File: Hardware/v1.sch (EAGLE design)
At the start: 75 parts, among them IC1 LM324D, IC2 m328p, IC3 REG1117, J1 22-27-2061-06, J2 22-27-2021-02, J3 22-27-2021-02, J4 22-27-2031-03, J5 22-27-2041-04, Q1 BSS123, Q2 BSS123, Q3 BSS123, Q5 BSS123

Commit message: slight changes in the layout
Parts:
- C9: value (none) -> 1000u
- L1, L2: device rcl:L-EUL2012C -> rcl:L-EUL2825P
- U$1: device IRF7424:IRF7424 -> MyLib:IRF7424
- U$3: value ELKO-1,27-4,2 -> 330u; device MyLib:ELKO-1,27-4,2 -> rcl:CPOL-EUE2-5
- U$4: value ELKO-1,27-4,2 -> 330u; device MyLib:ELKO-1,27-4,2 -> rcl:CPOL-EUE3.5-8
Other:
- moved on the sheet: C9, U$1
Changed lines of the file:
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@@
 <?xml version="1.0" encoding="utf-8"?>
 <!DOCTYPE eagle SYSTEM "eagle.dtd">
-<eagle version="6.6.0">
+<eagle version="6.5.0">
 <drawing>
 <settings>
@@
 <part name="S4" library="switch-omron" deviceset="10-XX" device=""/>
 <part name="GND4" library="supply1" deviceset="GND" device=""/>
-<part name="U$1" library="IRF7424" deviceset="IRF7424" device=""/>
+<part name="U$1" library="MyLib" deviceset="IRF7424" device=""/>
 <part name="U$2" library="3x7segCC" deviceset="3X7SEG" device=""/>
 <part name="GND5" library="supply1" deviceset="GND" device=""/>
@@
 <part name="R6" library="rcl" deviceset="R-EU_" device="R0402" value="10k"/>
 <part name="R7" library="rcl" deviceset="R-EU_" device="R0402" value="10k"/>
-<part name="U$3" library="MyLib" deviceset="ELKO-1,27-4,2" device=""/>
+<part name="U$3" library="rcl" deviceset="CPOL-EU" device="E2-5" value="330u"/>
 <part name="TP1" library="testpad" deviceset="PTR1" device="B1,27"/>
 <part name="TP2" library="testpad" deviceset="PTR1" device="B1,27"/>
@@
 <part name="TP5" library="testpad" deviceset="PTR1" device="B1,27"/>
 <part name="GND3" library="supply1" deviceset="GND" device=""/>
-<part name="L1" library="rcl" deviceset="L-EU" device="L2012C" value="10u"/>
-<part name="L2" library="rcl" deviceset="L-EU" device="L2012C" value="10u"/>
+<part name="L1" library="rcl" deviceset="L-EU" device="L2825P" value="10u"/>
+<part name="L2" library="rcl" deviceset="L-EU" device="L2825P" value="10u"/>
 <part name="C2" library="rcl" deviceset="C-EU" device="C0603" value="100n"/>
 <part name="GND12" library="supply1" deviceset="GND" device=""/>
@@
 <part name="TP9" library="testpad" deviceset="PTR1" device="B1,27"/>
 <part name="TP10" library="testpad" deviceset="PTR1" device="B1,27"/>
-<part name="C9" library="rcl" deviceset="CPOL-EU" device="E5-13"/>
+<part name="C9" library="rcl" deviceset="CPOL-EU" device="E5-13" value="1000u"/>
 <part name="R24" library="rcl" deviceset="R-EU_" device="R0603" value="750k"/>
 <part name="R25" library="rcl" deviceset="R-EU_" device="R0603" value="1k2"/>
@@
 <part name="J5" library="con-molex" deviceset="22-?-04" device="27-2041"/>
 <part name="J2" library="con-molex" deviceset="22-?-02" device="27-2021"/>
-<part name="U$4" library="MyLib" deviceset="ELKO-1,27-4,2" device=""/>
+<part name="U$4" library="rcl" deviceset="CPOL-EU" device="E3.5-8" value="330u"/>
 </parts>
 <sheets>
@@
 <instance part="S4" gate="1" x="304.8" y="238.76" rot="R270"/>
 <instance part="GND4" gate="1" x="210.82" y="200.66"/>
-<instance part="U$1" gate="G$1" x="190.5" y="223.52"/>
+<instance part="U$1" gate="G$1" x="167.64" y="208.28"/>
 <instance part="U$2" gate="G$1" x="223.52" y="48.26"/>
 <instance part="GND5" gate="1" x="76.2" y="218.44"/>
@@
 <instance part="TP9" gate="G$1" x="124.46" y="114.3" rot="R270"/>
 <instance part="TP10" gate="G$1" x="124.46" y="116.84" rot="R270"/>
-<instance part="C9" gate="G$1" x="180.34" y="210.82"/>
+<instance part="C9" gate="G$1" x="177.8" y="210.82"/>
 <instance part="IC1" gate="B" x="58.42" y="5.08"/>
 <instance part="R24" gate="G$1" x="55.88" y="-7.62"/>
@@
 <pinref part="J1" gate="-3" pin="S"/>
 <pinref part="C9" gate="G$1" pin="-"/>
-<wire x1="180.34" y1="205.74" x2="210.82" y2="205.74" width="0.1524" layer="91"/>
+<wire x1="177.8" y1="205.74" x2="210.82" y2="205.74" width="0.1524" layer="91"/>
 <junction x="210.82" y="205.74"/>
 <pinref part="C12" gate="G$1" pin="2"/>
-<wire x1="180.34" y1="205.74" x2="172.72" y2="205.74" width="0.1524" layer="91"/>
-<junction x="180.34" y="205.74"/>
+<wire x1="177.8" y1="205.74" x2="172.72" y2="205.74" width="0.1524" layer="91"/>
+<junction x="177.8" y="205.74"/>
 </segment>
 <segment>
@@
 <wire x1="177.8" y1="226.06" x2="177.8" y2="220.98" width="0.1524" layer="91"/>
 <junction x="177.8" y="220.98"/>
-<wire x1="177.8" y1="220.98" x2="180.34" y2="213.36" width="0.1524" layer="91"/>
+<wire x1="177.8" y1="220.98" x2="177.8" y2="218.44" width="0.1524" layer="91"/>
 <pinref part="C12" gate="G$1" pin="1"/>
-<wire x1="172.72" y1="213.36" x2="180.34" y2="213.36" width="0.1524" layer="91"/>
-<junction x="180.34" y="213.36"/>
+<wire x1="172.72" y1="213.36" x2="177.8" y2="213.36" width="0.1524" layer="91"/>
+<junction x="177.8" y="213.36"/>
+<wire x1="177.8" y1="218.44" x2="180.34" y2="218.44" width="0.1524" layer="91"/>
+<wire x1="180.34" y1="218.44" x2="180.34" y2="213.36" width="0.1524" layer="91"/>
+<wire x1="180.34" y1="213.36" x2="177.8" y2="213.36" width="0.1524" layer="91"/>
 </segment>
 </net>
@@
 <wire x1="208.28" y1="213.36" x2="218.44" y2="213.36" width="0.1524" layer="91"/>
 <pinref part="U$1" gate="G$1" pin="D1"/>
+<wire x1="200.66" y1="231.14" x2="203.2" y2="231.14" width="0.1524" layer="91"/>
 <pinref part="U$1" gate="G$1" pin="D2"/>
+<wire x1="200.66" y1="226.06" x2="203.2" y2="226.06" width="0.1524" layer="91"/>
 <junction x="203.2" y="226.06"/>
 <pinref part="U$1" gate="G$1" pin="D3"/>
+<wire x1="200.66" y1="220.98" x2="203.2" y2="220.98" width="0.1524" layer="91"/>
 <junction x="203.2" y="220.98"/>
 <pinref part="U$1" gate="G$1" pin="D4"/>
+<wire x1="200.66" y1="215.9" x2="203.2" y2="215.9" width="0.1524" layer="91"/>
 <wire x1="218.44" y1="215.9" x2="218.44" y2="213.36" width="0.1524" layer="91"/>
 <pinref part="LED1" gate="G$1" pin="A"/>

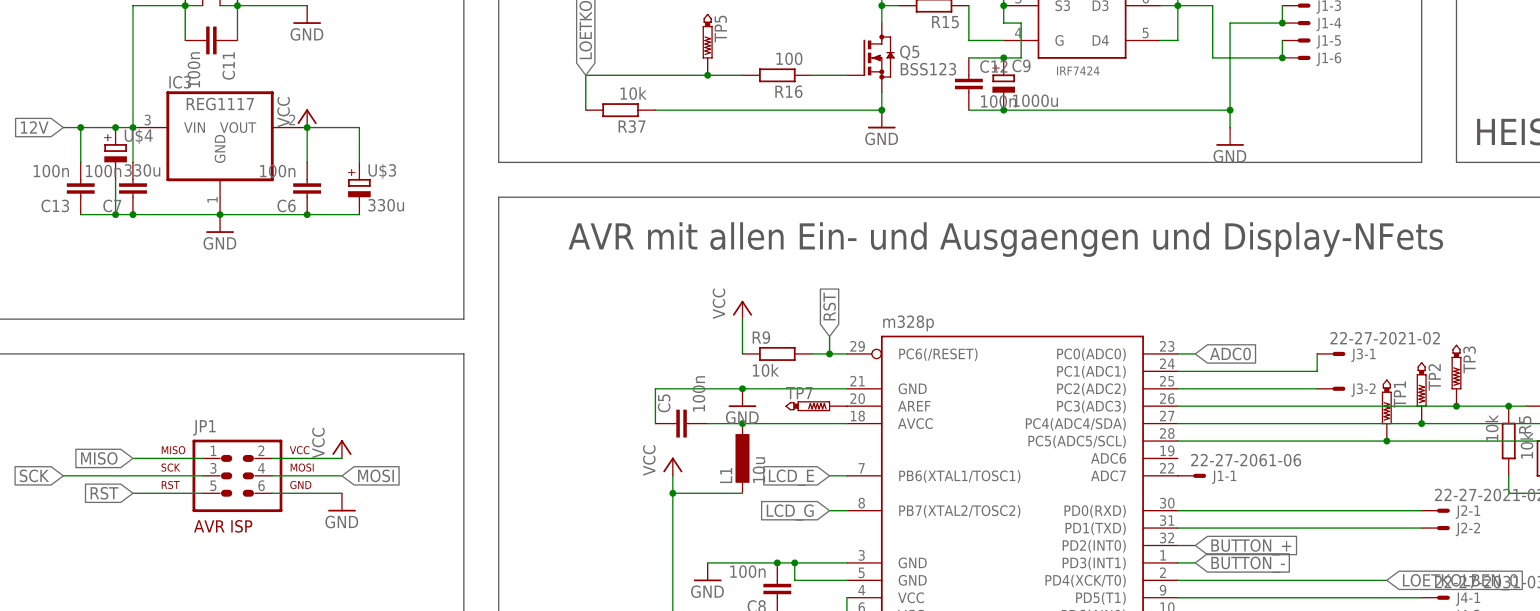
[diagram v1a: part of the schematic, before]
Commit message: finish layer done so pcb will have the components names printed on it
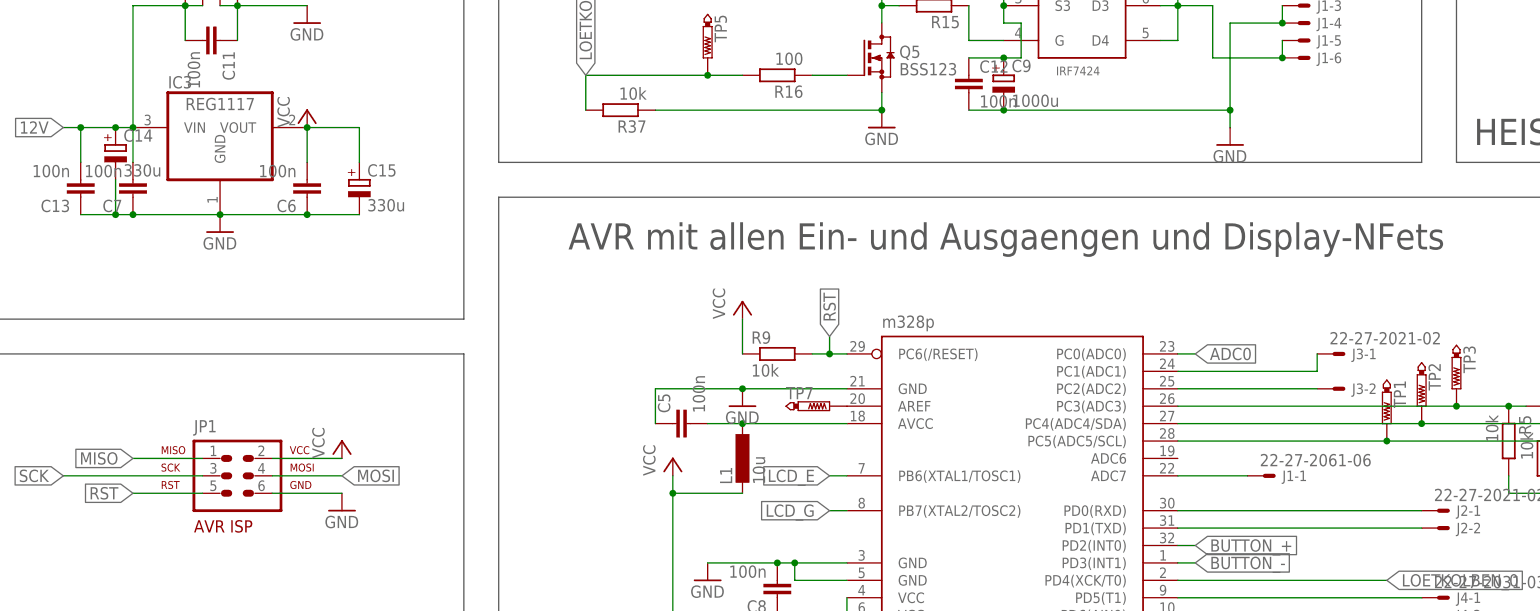
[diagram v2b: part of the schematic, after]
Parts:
- renumbered U$3 to C15, U$4 to C14
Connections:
- net N$27 renamed ADC7
- net N$28 renamed ADC1
- net N$29 renamed ADC2
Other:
- moved on the sheet: J1-1
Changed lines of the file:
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@@
 <part name="R6" library="rcl" deviceset="R-EU_" device="R0402" value="10k"/>
 <part name="R7" library="rcl" deviceset="R-EU_" device="R0402" value="10k"/>
-<part name="U$3" library="rcl" deviceset="CPOL-EU" device="E2-5" value="330u"/>
+<part name="C15" library="rcl" deviceset="CPOL-EU" device="E2-5" value="330u"/>
 <part name="TP1" library="testpad" deviceset="PTR1" device="B1,27"/>
 <part name="TP2" library="testpad" deviceset="PTR1" device="B1,27"/>
@@
 <part name="J5" library="con-molex" deviceset="22-?-04" device="27-2041"/>
 <part name="J2" library="con-molex" deviceset="22-?-02" device="27-2021"/>
-<part name="U$4" library="rcl" deviceset="CPOL-EU" device="E3.5-8" value="330u"/>
+<part name="C14" library="rcl" deviceset="CPOL-EU" device="E3.5-8" value="330u"/>
 </parts>
 <sheets>
@@
 <instance part="R6" gate="G$1" x="256.54" y="154.94" rot="R270"/>
 <instance part="R7" gate="G$1" x="261.62" y="152.4" rot="R270"/>
-<instance part="U$3" gate="G$1" x="83.82" y="195.58"/>
+<instance part="C15" gate="G$1" x="83.82" y="195.58"/>
 <instance part="TP1" gate="G$1" x="233.68" y="160.02" rot="R180"/>
 <instance part="TP2" gate="G$1" x="238.76" y="162.56" rot="R180"/>
@@
 <instance part="R26" gate="G$1" x="208.28" y="238.76" rot="R180"/>
 <instance part="GND18" gate="1" x="213.36" y="236.22"/>
-<instance part="J1" gate="-1" x="205.74" y="152.4"/>
+<instance part="J1" gate="-1" x="215.9" y="152.4"/>
 <instance part="J1" gate="-2" x="220.98" y="223.52"/>
 <instance part="J1" gate="-3" x="220.98" y="220.98"/>
@@
 <instance part="J2" gate="-1" x="241.3" y="147.32"/>
 <instance part="J2" gate="-2" x="241.3" y="144.78"/>
-<instance part="U$4" gate="G$1" x="48.26" y="200.66"/>
+<instance part="C14" gate="G$1" x="48.26" y="200.66"/>
 </instances>
 <busses>
@@
 <pinref part="P+5" gate="VCC" pin="VCC"/>
 <junction x="76.2" y="203.2"/>
-<pinref part="U$3" gate="G$1" pin="+"/>
+<pinref part="C15" gate="G$1" pin="+"/>
 <wire x1="76.2" y1="203.2" x2="83.82" y2="203.2" width="0.1524" layer="91"/>
 <wire x1="83.82" y1="203.2" x2="83.82" y2="198.12" width="0.1524" layer="91"/>
@@
 <junction x="63.5" y="190.5"/>
 <pinref part="GND15" gate="1" pin="GND"/>
-<pinref part="U$3" gate="G$1" pin="-"/>
+<pinref part="C15" gate="G$1" pin="-"/>
 <wire x1="83.82" y1="190.5" x2="76.2" y2="190.5" width="0.1524" layer="91"/>
 <junction x="76.2" y="190.5"/>
@@
 <wire x1="43.18" y1="190.5" x2="48.26" y2="190.5" width="0.1524" layer="91"/>
 <junction x="50.8" y="190.5"/>
-<pinref part="U$4" gate="G$1" pin="-"/>
+<pinref part="C14" gate="G$1" pin="-"/>
 <wire x1="48.26" y1="190.5" x2="50.8" y2="190.5" width="0.1524" layer="91"/>
 <wire x1="48.26" y1="195.58" x2="48.26" y2="190.5" width="0.1524" layer="91"/>
@@
 <pinref part="J5" gate="-1" pin="S"/>
 <pinref part="J5" gate="-2" pin="S"/>
-<pinref part="U$4" gate="G$1" pin="+"/>
+<pinref part="C14" gate="G$1" pin="+"/>
 <junction x="48.26" y="203.2"/>
 </segment>
@@
 </segment>
 </net>
-<net name="N$27" class="0">
+<net name="ADC7" class="0">
 <segment>
 <pinref part="IC2" gate="G$1" pin="ADC7"/>
 <pinref part="J1" gate="-1" pin="S"/>
-</segment>
-</net>
-<net name="N$28" class="0">
+<wire x1="213.36" y1="152.4" x2="203.2" y2="152.4" width="0.1524" layer="91"/>
+</segment>
+</net>
+<net name="ADC1" class="0">
 <segment>
 <pinref part="IC2" gate="G$1" pin="PC1(ADC1)"/>
@@
 </segment>
 </net>
-<net name="N$29" class="0">
+<net name="ADC2" class="0">
 <segment>
 <pinref part="J3" gate="-2" pin="S"/>

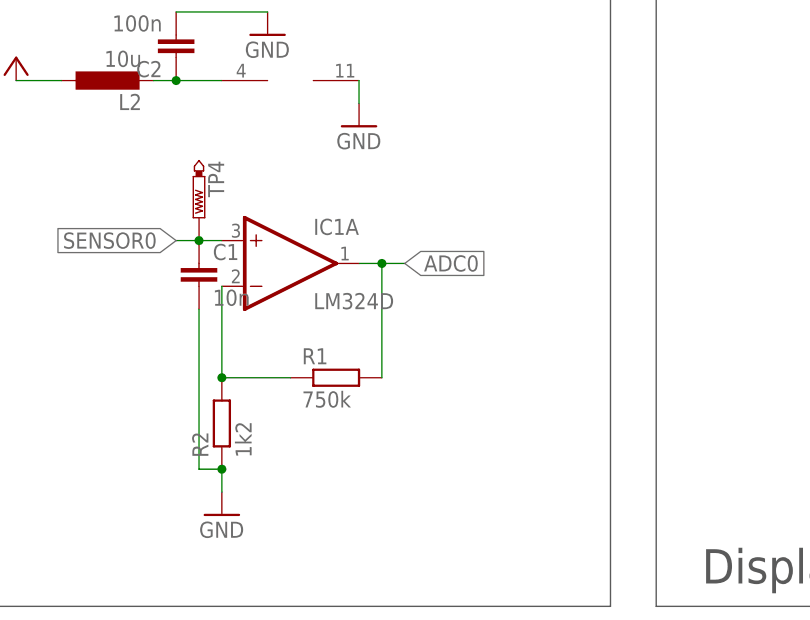
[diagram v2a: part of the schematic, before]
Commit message: op-amp rework
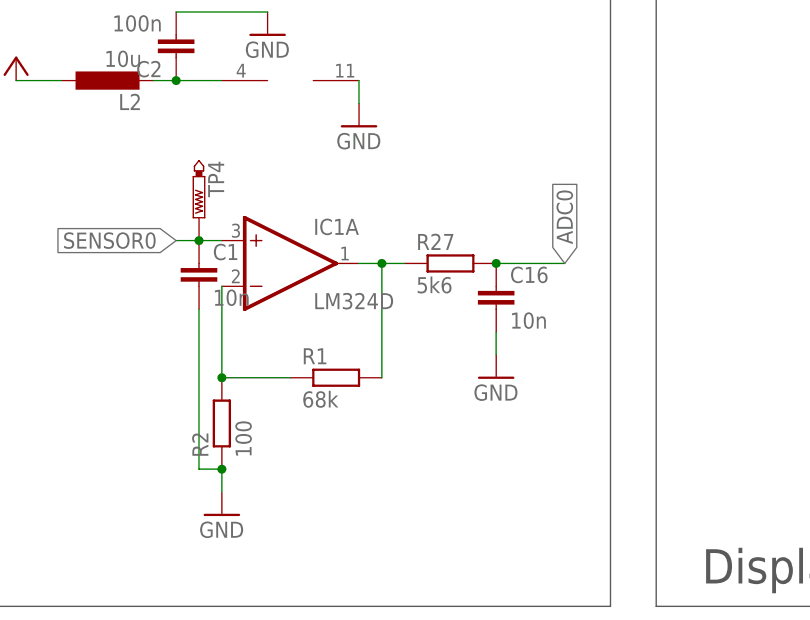
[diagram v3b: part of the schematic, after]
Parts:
- added C16: 10n, rcl:C-EUC0603
- added R27: 5k6, rcl:R-EU_R0603
- R1: value 750k -> 68k
- R2: value 1k2 -> 100
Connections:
- new net SDFGHJK: IC1A.OUT, R1.2, R27.1
- net ADC0: now also C16.1, R27.2; no longer IC1A.OUT, R1.2
- net GND: now also C16.2
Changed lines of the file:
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@@
 <part name="P+1" library="supply1" deviceset="VCC" device=""/>
 <part name="GND1" library="supply1" deviceset="GND" device=""/>
-<part name="R2" library="rcl" deviceset="R-EU_" device="R0603" value="1k2"/>
-<part name="R1" library="rcl" deviceset="R-EU_" device="R0603" value="750k"/>
+<part name="R2" library="rcl" deviceset="R-EU_" device="R0603" value="100"/>
+<part name="R1" library="rcl" deviceset="R-EU_" device="R0603" value="68k"/>
 <part name="GND2" library="supply1" deviceset="GND" device=""/>
 <part name="C1" library="rcl" deviceset="C-EU" device="C0603" value="10n"/>
@@
 <part name="J2" library="con-molex" deviceset="22-?-02" device="27-2021"/>
 <part name="C14" library="rcl" deviceset="CPOL-EU" device="E3.5-8" value="330u"/>
+<part name="C16" library="rcl" deviceset="C-EU" device="C0603" value="10n"/>
+<part name="GND17" library="supply1" deviceset="GND" device=""/>
+<part name="R27" library="rcl" deviceset="R-EU_" device="R0603" value="5k6"/>
 </parts>
 <sheets>
@@
 <instance part="J2" gate="-2" x="241.3" y="144.78"/>
 <instance part="C14" gate="G$1" x="48.26" y="200.66"/>
+<instance part="C16" gate="G$1" x="86.36" y="63.5"/>
+<instance part="GND17" gate="1" x="86.36" y="53.34"/>
+<instance part="R27" gate="G$1" x="81.28" y="66.04"/>
 </instances>
 <busses>
@@
 <wire x1="43.18" y1="-7.62" x2="43.18" y2="-5.08" width="0.1524" layer="91"/>
 </segment>
+<segment>
+<pinref part="C16" gate="G$1" pin="2"/>
+<pinref part="GND17" gate="1" pin="GND"/>
+<wire x1="86.36" y1="58.42" x2="86.36" y2="55.88" width="0.1524" layer="91"/>
+</segment>
 </net>
 <net name="N$1" class="0">
@@
 <net name="ADC0" class="0">
 <segment>
-<label x="76.2" y="66.04" size="1.778" layer="95" xref="yes"/>
-<pinref part="IC1" gate="A" pin="OUT"/>
-<pinref part="R1" gate="G$1" pin="2"/>
-<wire x1="73.66" y1="66.04" x2="73.66" y2="53.34" width="0.1524" layer="91"/>
-<wire x1="73.66" y1="66.04" x2="71.12" y2="66.04" width="0.1524" layer="91"/>
-<wire x1="73.66" y1="66.04" x2="76.2" y2="66.04" width="0.1524" layer="91"/>
-<junction x="73.66" y="66.04"/>
-</segment>
-<segment>
 <pinref part="IC2" gate="G$1" pin="PC0(ADC0)"/>
 <wire x1="203.2" y1="170.18" x2="205.74" y2="170.18" width="0.1524" layer="91"/>
 <label x="205.74" y="170.18" size="1.778" layer="95" xref="yes"/>
+</segment>
+<segment>
+<pinref part="C16" gate="G$1" pin="1"/>
+<wire x1="86.36" y1="66.04" x2="93.98" y2="66.04" width="0.1524" layer="91"/>
+<junction x="86.36" y="66.04"/>
+<pinref part="R27" gate="G$1" pin="2"/>
+<label x="93.98" y="66.04" size="1.778" layer="95" rot="R90" xref="yes"/>
 </segment>
 </net>
@@
 </segment>
 </net>
+<net name="SDFGHJK" class="0">
+<segment>
+<pinref part="IC1" gate="A" pin="OUT"/>
+<pinref part="R1" gate="G$1" pin="2"/>
+<wire x1="73.66" y1="66.04" x2="73.66" y2="53.34" width="0.1524" layer="91"/>
+<wire x1="73.66" y1="66.04" x2="71.12" y2="66.04" width="0.1524" layer="91"/>
+<wire x1="73.66" y1="66.04" x2="76.2" y2="66.04" width="0.1524" layer="91"/>
+<junction x="73.66" y="66.04"/>
+<pinref part="R27" gate="G$1" pin="1"/>
+</segment>
+</net>

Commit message: latest version with some updates
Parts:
- added AREF: PTR1B1,27, testpad:PTR1B1,27
- R1: value 68k -> 43k
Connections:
- net ADC0 renamed THERMO0
- net ADC1 renamed HALL
- removed net N$24: IC2.AREF, TP7.TP
- new net AREF: AREF.TP, IC2.AREF
- net ADC2: now also TP7.TP; no longer J3-2.S
- net VCC: now also J3-2.S
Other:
- note added: "For Future Use"
- note added: "OpAmp für das Thermo- element im Loetkolben Verstaerkung 431"
- note removed: "OpAmp für das Thermo- element im Loetkolben"
- moved on the sheet: C1, C10, C16, C2, IC1B, J3-2, L2, R1, R24, R25, TP11, TP12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
